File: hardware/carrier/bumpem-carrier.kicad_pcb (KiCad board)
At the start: 2 copper layers, 120 x 93.5 mm, 22 parts, among them J1 Module A, J2 Module B, J3 Module C, J4 Module D, U1 Teensy 4.1, U2 MCP4728 (Adafruit 4470)

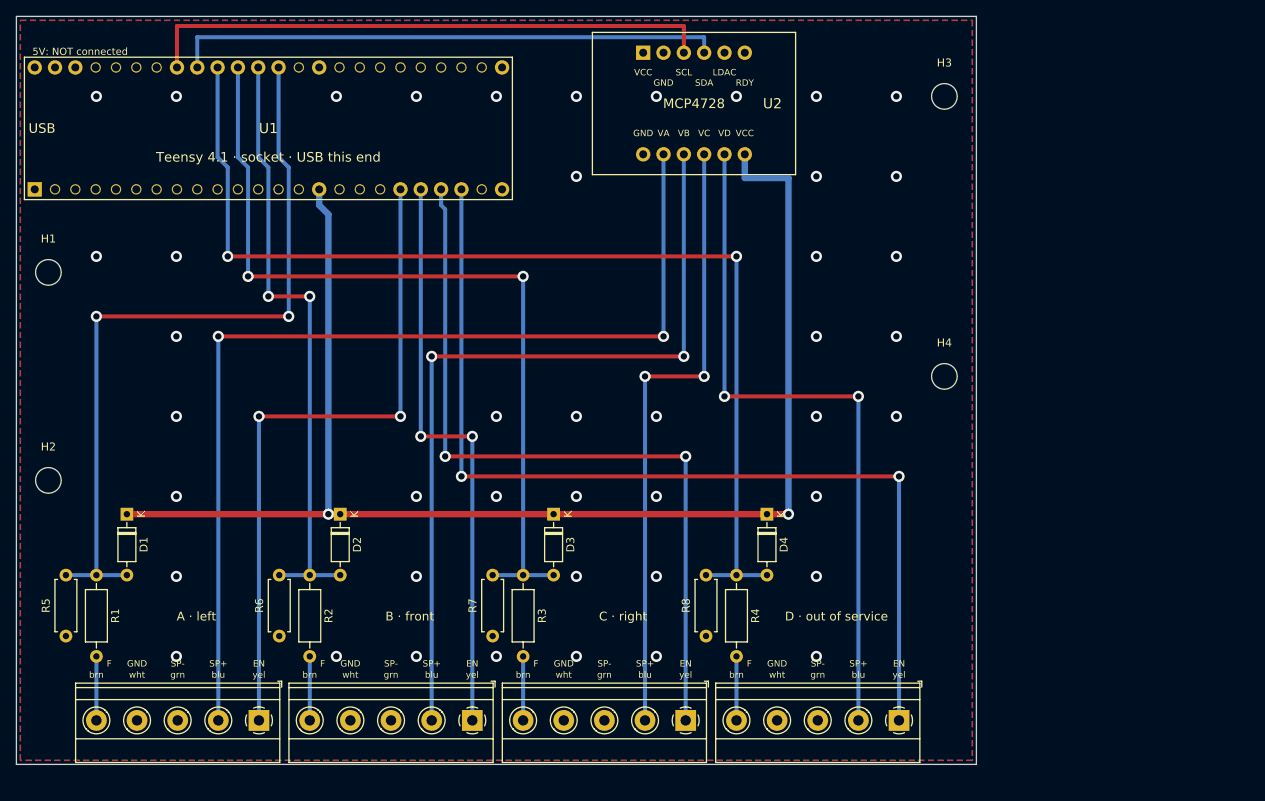
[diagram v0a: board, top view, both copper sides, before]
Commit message: docs: carrier board spacing (force tracks clear of socket pins, gaps >= 0.74 mm), module D active
Co-Authored-By: Claude Opus 5.5 <noreply@anthropic.com>
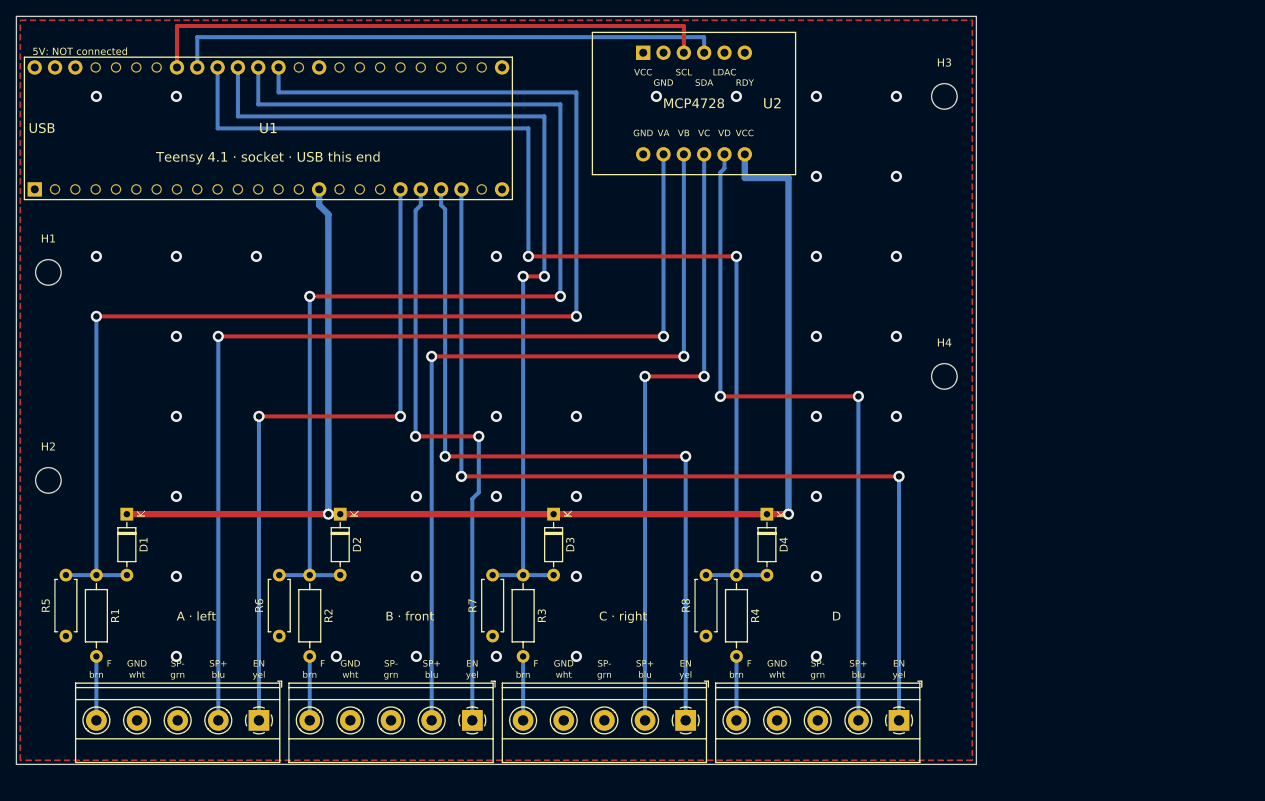
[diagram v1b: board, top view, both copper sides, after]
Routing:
- net F_A: track 95.6 -> 168.3 mm
- net F_B: track 76.8 -> 140.2 mm
- net F_C: track 106.0 -> 112.1 mm
- net EN_B: track 72.8 -> 74.9 mm
- net F_D: track 135.2 -> 135.9 mm
- net SP_D: track 87.5 -> 88.2 mm
- net GND: vias 44 -> 37
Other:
- board text added: "D"
- board text added: "Teensy 4.1 + MCP4728 → modules A-D"
- board text removed: "D · out of service"
- board text removed: "Teensy 4.1 + MCP4728 → modules A-D (D out of service)"

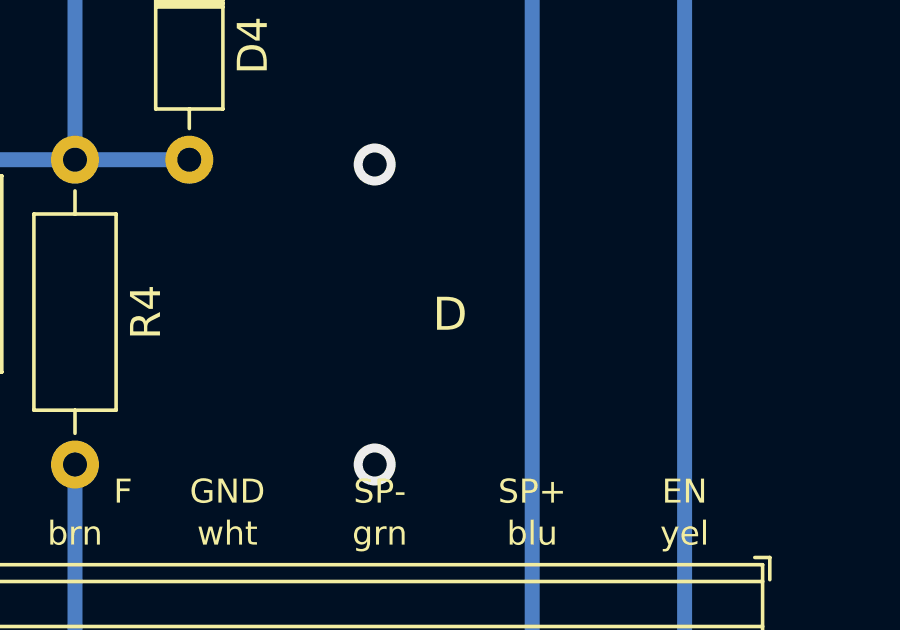
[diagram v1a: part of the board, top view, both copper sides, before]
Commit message: api: perturbation by angle (Vicon axes, split over neighbouring cables), geometry endpoint, bumpem perturb; module D back
Co-Authored-By: Claude Opus 5.5 <noreply@anthropic.com>
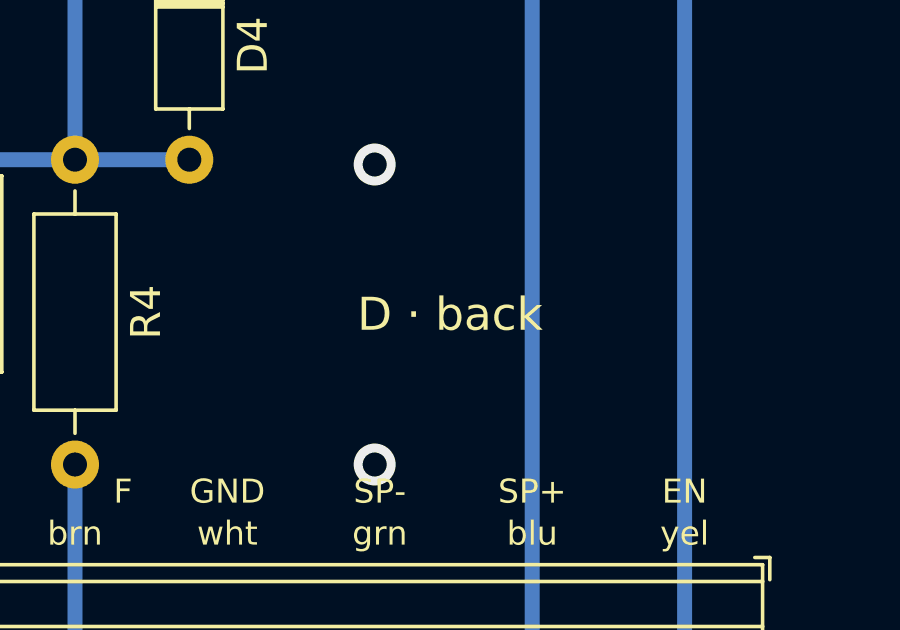
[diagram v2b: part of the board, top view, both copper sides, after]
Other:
- board text added: "D · back"
- board text removed: "D"

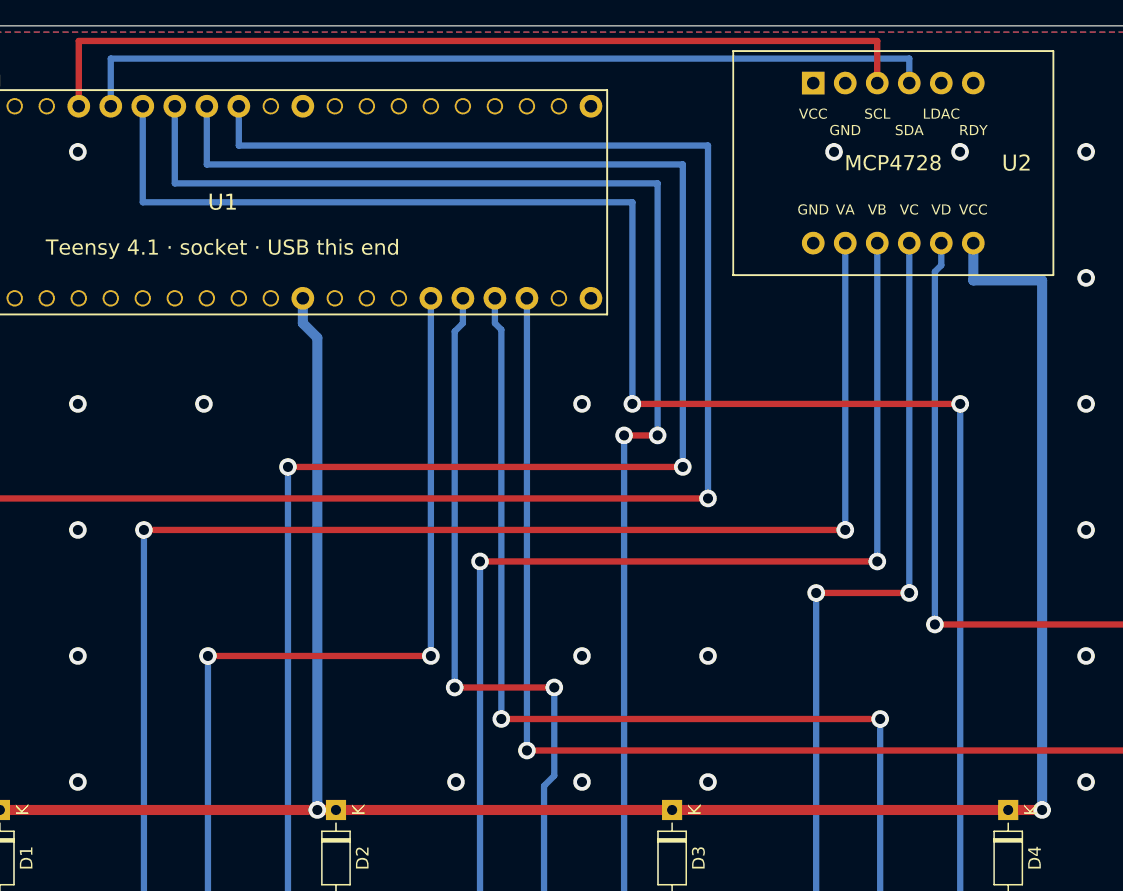
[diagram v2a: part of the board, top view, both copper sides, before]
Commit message: docs: carrier board 45 deg bends, 0.5 mm pour gap, top/bottom PDFs + KiCad zip (makerspace review)
Co-Authored-By: Claude Opus 5.5 <noreply@anthropic.com>
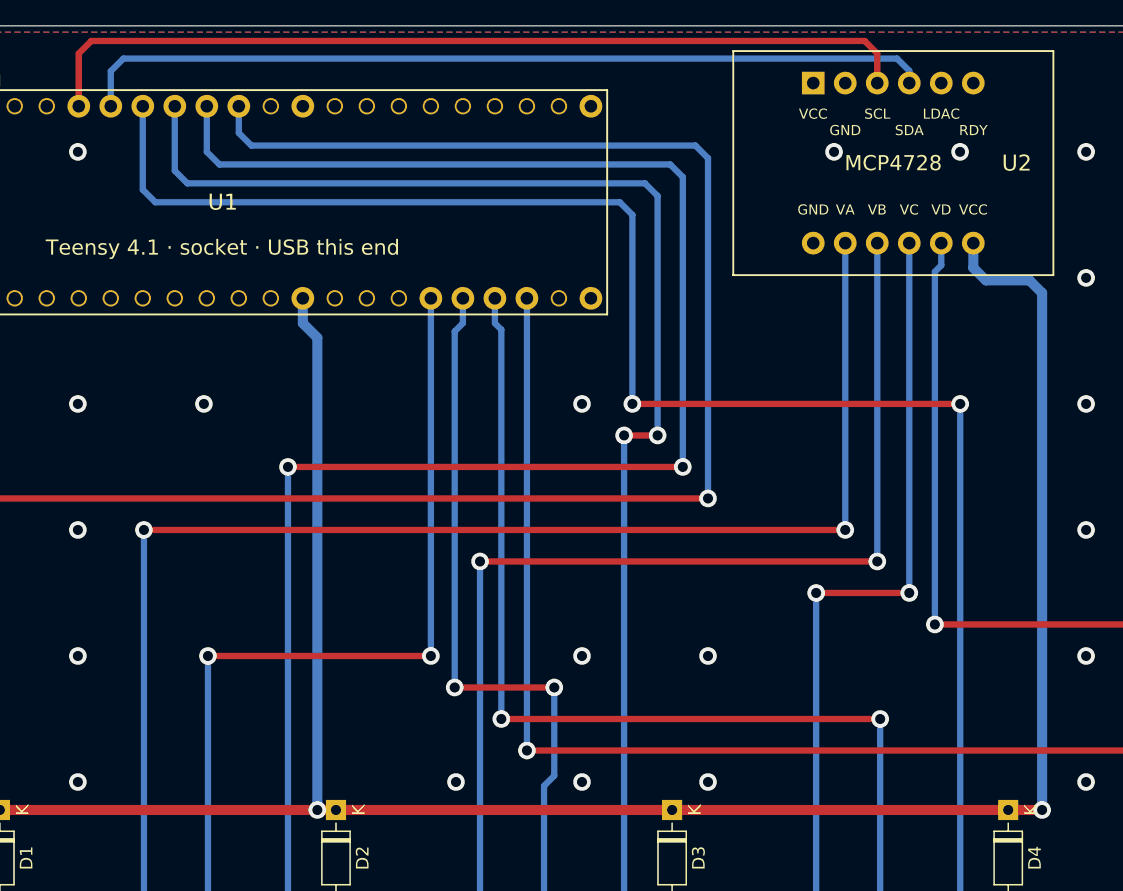
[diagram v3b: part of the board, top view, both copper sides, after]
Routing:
- net F_B: track 140.2 -> 139.0 mm
- net F_D: track 135.9 -> 134.8 mm
- net F_A: track 168.3 -> 167.1 mm
- net SCL: track 71.9 -> 70.7 mm
- net F_C: track 112.1 -> 110.9 mm
- net +3V3: track 174.2 -> 173.0 mm
- net SDA: track 69.1 -> 67.9 mm

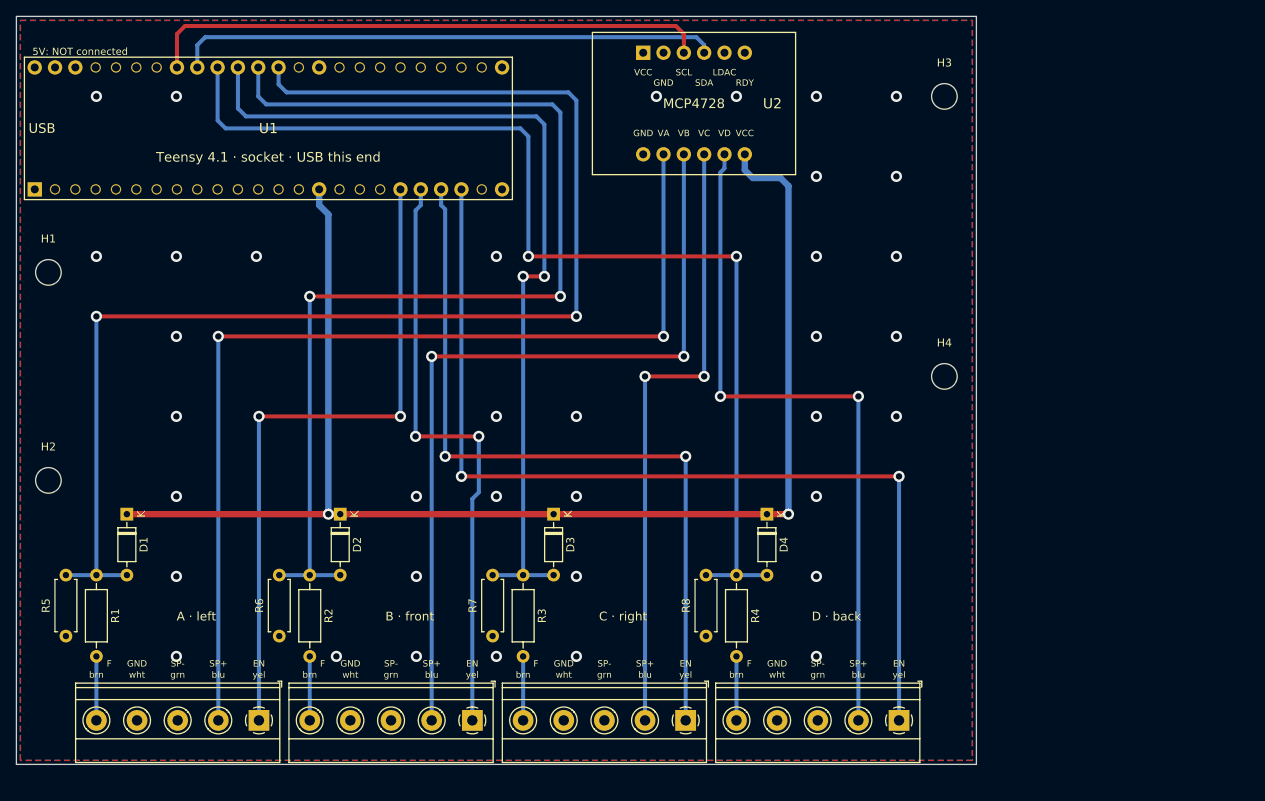
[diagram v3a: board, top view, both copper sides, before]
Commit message: docs: carrier board pluggable module connectors (Phoenix MSTB 2,5 with flanges), board 154 x 96 mm
Co-Authored-By: Claude Opus 5.5 <noreply@anthropic.com>
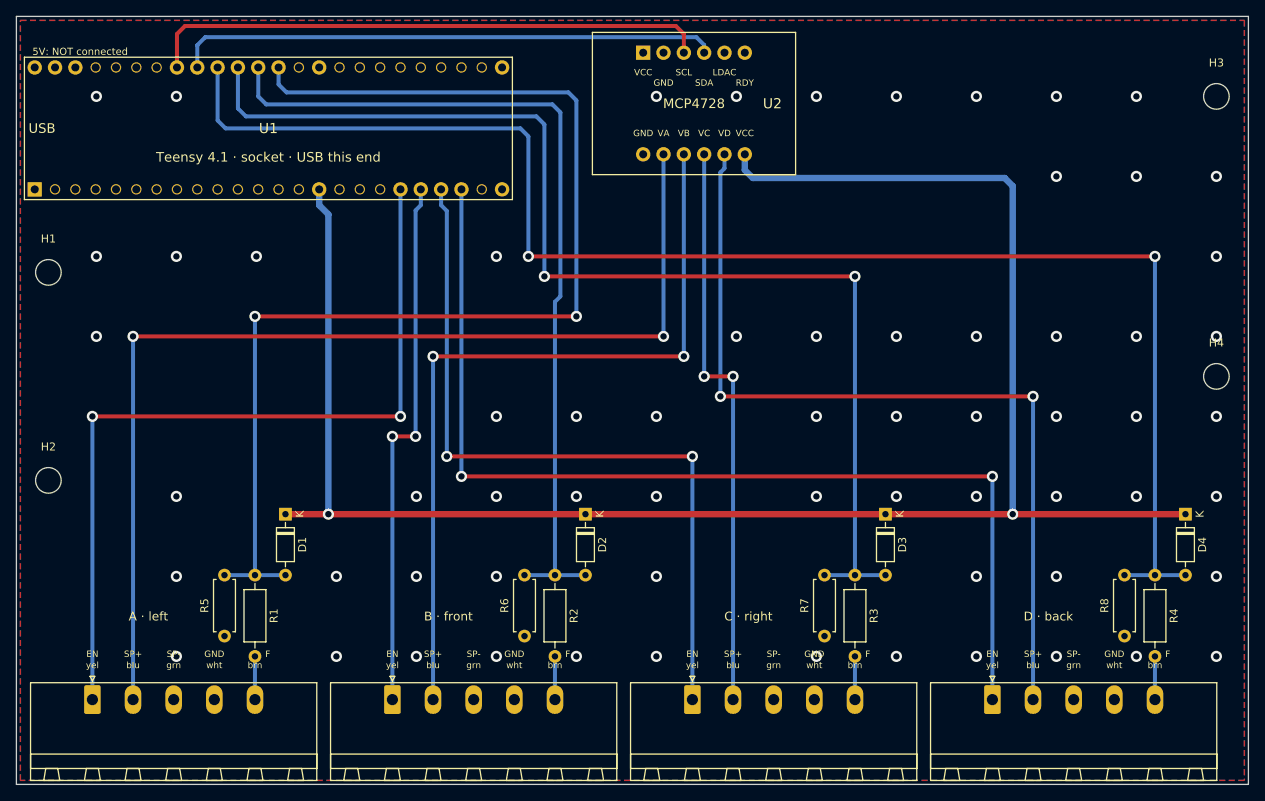
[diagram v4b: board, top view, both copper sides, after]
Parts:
- J1, J2, J3, J4: footprint TerminalBlock_Phoenix:TerminalBlock_Phoenix_MKDS-1,5-5-5.08_1x05_P5.08mm_Horizontal -> Connector_Phoenix_MSTB:PhoenixContact_MSTB_2,5_5-GF-5,08_1x05_P5.08mm_Horizontal_ThreadedFlange
- moved D4 52.3 mm to (146.1, 62.2)
- moved R4 52.3 mm to (142.3, 69.8)
- moved R8 52.3 mm to (138.5, 69.8)
- moved D3 41.5 mm to (108.6, 62.2)
- moved R7 41.5 mm to (101.0, 69.8)
- moved R3 41.5 mm to (104.8, 69.8)
- moved H3 34.0 mm to (150.0, 10.0)
- moved H4 34.0 mm to (150.0, 45.0)
- moved D2 30.6 mm to (71.1, 62.2)
- moved R2 30.6 mm to (67.3, 69.8)
- moved R6 30.6 mm to (63.5, 69.8)
- moved J1 21.0 mm to (9.50, 85.4), turned to 0 degrees
- moved R5 19.8 mm to (26.0, 69.8)
- moved D1 19.8 mm to (33.6, 62.2)
- moved R1 19.8 mm to (29.8, 69.8)
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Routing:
- net +3V3: track 173.0 -> 230.9 mm
- net F_D: track 134.8 -> 187.1 mm
- net F_C: track 110.9 -> 147.0 mm
- net F_B: track 139.0 -> 108.0 mm, vias 2 -> 0
- net F_A: track 167.1 -> 147.3 mm
- net SP_D: track 88.2 -> 107.5 mm
- net EN_A: track 84.1 -> 102.3 mm
- net EN_D: track 121.1 -> 130.2 mm
- net SP_A: track 126.4 -> 134.5 mm
- net EN_B: track 74.9 -> 66.9 mm
- net SP_C: track 78.2 -> 71.8 mm
- net SP_B: track 102.3 -> 99.5 mm
- net FIN_D: track 8.00 -> 5.40 mm
- net FIN_C: track 8.00 -> 5.40 mm
- net FIN_B: track 8.00 -> 5.40 mm
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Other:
- board size 120 x 93.5 mm -> 154 x 96 mm
- board text added: "module plugs (Phoenix MSTB 2,5/5-STF-5,08) at the bottom edge"
- board text removed: "module wires enter here ↓ (bottom edge)"
